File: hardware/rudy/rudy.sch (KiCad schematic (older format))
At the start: 20 parts, among them IC1 ATMEGA328-P, P1 CONN1, P2 CONN2, P3 SERPROG, P4 USB_B, U1 LD1117S33TR, Y1 Crystal

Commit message: Changed Zener diodes
Changed footprint for D1 and D2 Zener diodes from Mini MILF to SOD-323F
and moved their position in front of R1 and R2.

That came with a bit of rerouting, and trying to keep the pad position
close enough to the initial ones, so I don't have to order new stencils
right away (while even still waiting for them)
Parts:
- D1, D2: footprint Diodes_SMD:D_MiniMELF -> Diodes_SMD:D_SOD-323F
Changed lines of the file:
@@
 F 0 "D1" H 2400 4350 50  0000 C CNN
 F 1 "3V6" H 2400 4150 50  0000 C CNN
-F 2 "Diodes_SMD:D_MiniMELF" H 2400 4250 50  0001 C CNN
+F 2 "Diodes_SMD:D_SOD-323F" H 2400 4250 50  0001 C CNN
 F 3 "" H 2400 4250 50  0000 C CNN
 	1    2400 4250
@@
 F 0 "D2" H 2700 4350 50  0000 C CNN
 F 1 "3V6" H 2700 4150 50  0000 C CNN
-F 2 "Diodes_SMD:D_MiniMELF" H 2700 4250 50  0001 C CNN
+F 2 "Diodes_SMD:D_SOD-323F" H 2700 4250 50  0001 C CNN
 F 3 "" H 2700 4250 50  0000 C CNN
 	1    2700 4250

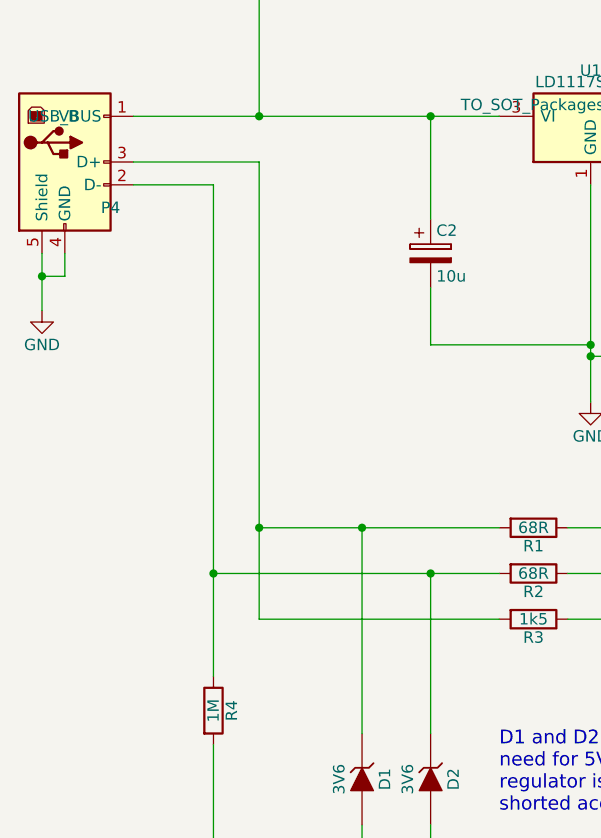
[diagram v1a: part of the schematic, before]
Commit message: Fixed USB-B component after KiCad update
Turns out 1-3-2-4-5 is a more logical pin arrangement for some people,
and I fucked up paying attention to this, so D+ and D- USB lines got
swapped in the schematic component. Should have been more suspicious
why I had to do so much re-routing after updating the Zener diodes.
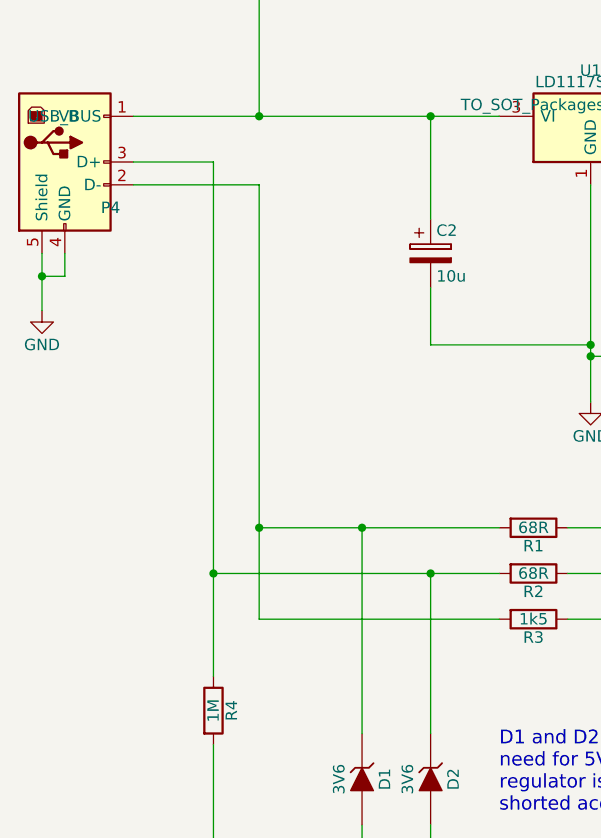
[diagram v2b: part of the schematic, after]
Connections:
- net at D2.1 (K), R2.2, R4.1: now also P4.3 (D+); no longer P4.2 (D-)
- net at D1.1 (K), R1.2, R3.2: now also P4.2 (D-); no longer P4.3 (D+)
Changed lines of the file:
@@
 	1950 750  1950 1350
 Connection ~ 1950 1350
-Wire Wire Line
-	1400 1650 1750 1650
-Wire Wire Line
-	1750 1650 1750 3800
-Wire Wire Line
-	1400 1550 1950 1550
-Wire Wire Line
-	1950 1550 1950 3550
-Connection ~ 1950 3150
 Connection ~ 1750 3350
 Wire Wire Line
@@
 	1100 2050 1000 2050
 Connection ~ 1000 2050
+Wire Wire Line
+	1950 1650 1950 3550
+Wire Wire Line
+	1750 1550 1750 3800
+Wire Wire Line
+	1400 1650 1950 1650
+Connection ~ 1950 3150
+Wire Wire Line
+	1400 1550 1750 1550
 $EndSCHEMATC

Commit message: HW: added LEDs and AVCC cap
There were no LEDs.
Why were there no LEDs?!
Everything needs LEDs!

So now there are, indicating that the device is actually powered, which
will lessen occasional confusion about that (especially when one forgets
to adjust the jumper after flashing).

But simple LED alone is boring, so there's now two below the IC itself,
giving a great glow to the device.

Note that this is really only just a power indication and not routed to
any output pin, so the LEDs are always on and can't be controlled by the
microcontroller itself -- at least at this point.

Also added 100nF cap to decouple VCC and AVCC, just in case.
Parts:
- added C6: 100n, Capacitor_SMD:C_0805_2012Metric, symbol rudy-rescue:C
- added D3, D4: LED, LED_SMD:LED_0805_2012Metric, symbol Device:LED
- added R5, R6: 120R, Resistor_SMD:R_0805_2012Metric, symbol Device:R
- C1, C4, C5: footprint Capacitors_SMD:C_0805 -> Capacitor_SMD:C_0805_2012Metric; symbol C -> rudy-rescue:C
- C2, C3: symbol CP -> rudy-rescue:CP
- D1, D2: symbol ZENER -> rudy-rescue:ZENER
- IC1: symbol ATMEGA328-P -> rudy-rescue:ATMEGA328-P
- JP1: symbol JUMPER3 -> rudy-rescue:JUMPER3
- JP2: symbol JUMPER -> rudy-rescue:JUMPER
- P1, P2: symbol CONN_01X14 -> rudy-rescue:CONN_01X14
- P3: symbol CONN_02X03 -> rudy-rescue:CONN_02X03
- P4: symbol USB_B -> rudy-rescue:USB_B
- R1, R2, R3, R4: footprint Resistors_SMD:R_0805 -> Resistor_SMD:R_0805_2012Metric; symbol R -> rudy-rescue:R
- U1: symbol LD1117S33TR -> rudy-rescue:LD1117S33TR
- Y1: symbol Crystal -> rudy-rescue:Crystal
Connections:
- net AVCC: now also C6.2
- net GND: now also D3.1 (K), D4.1 (K)
- net VCC: now also C6.1, R5.2, R6.2
- new net: D3.2 (A), R5.1
- new net: D4.2 (A), R6.1
